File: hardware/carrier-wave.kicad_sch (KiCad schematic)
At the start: 4 parts, among them U2 OPA695, U3 THS3491, U4 AD9834, U7 TS5A3159ADCK

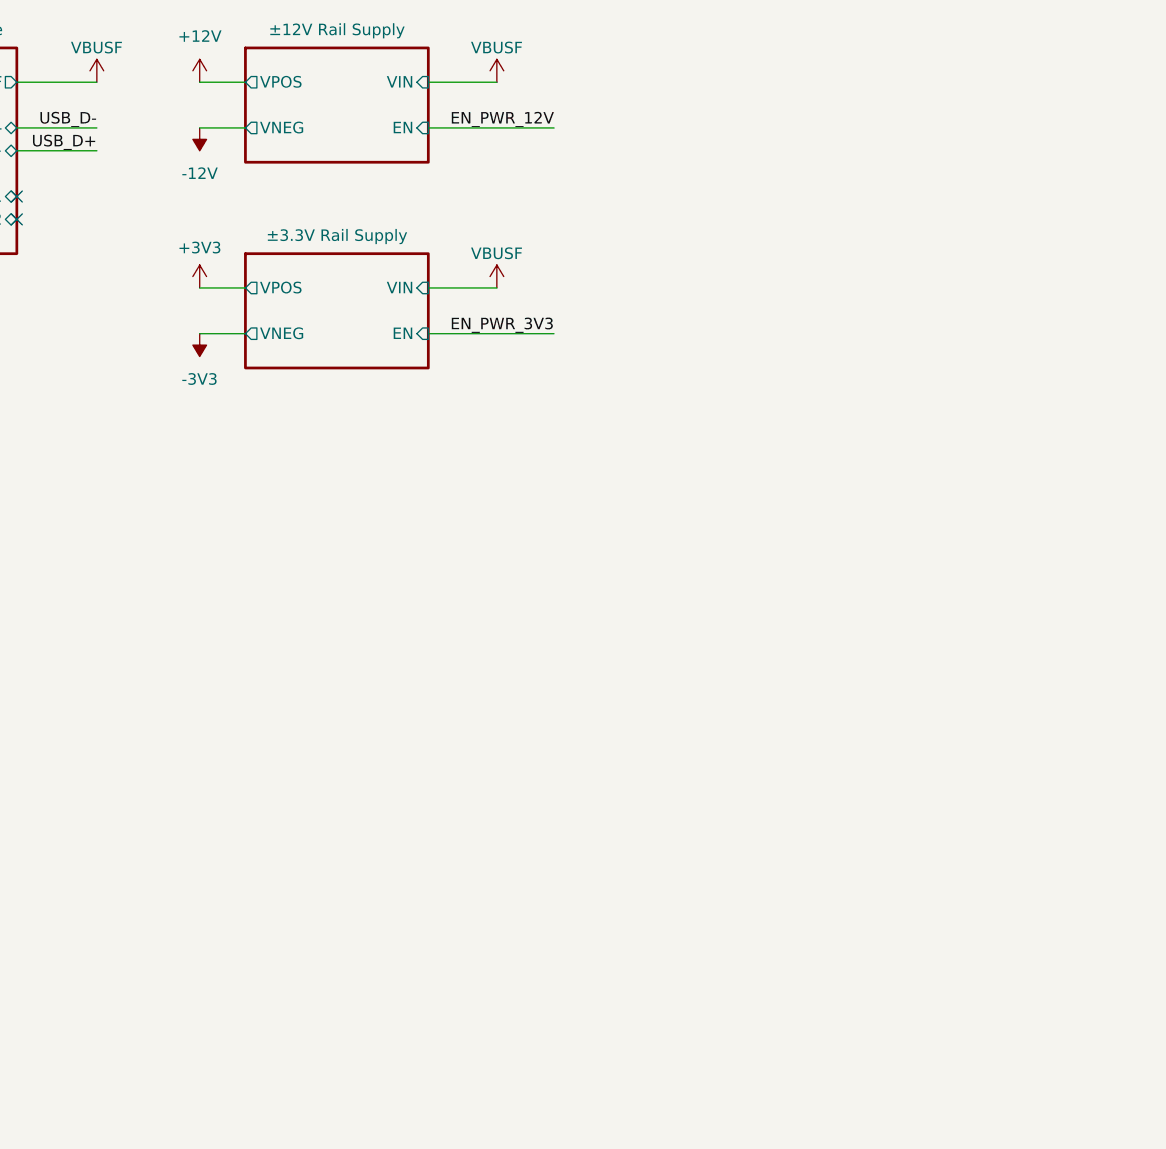
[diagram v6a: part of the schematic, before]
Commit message: Begin digital design
created sheets for MCU and 3.3VD regulator
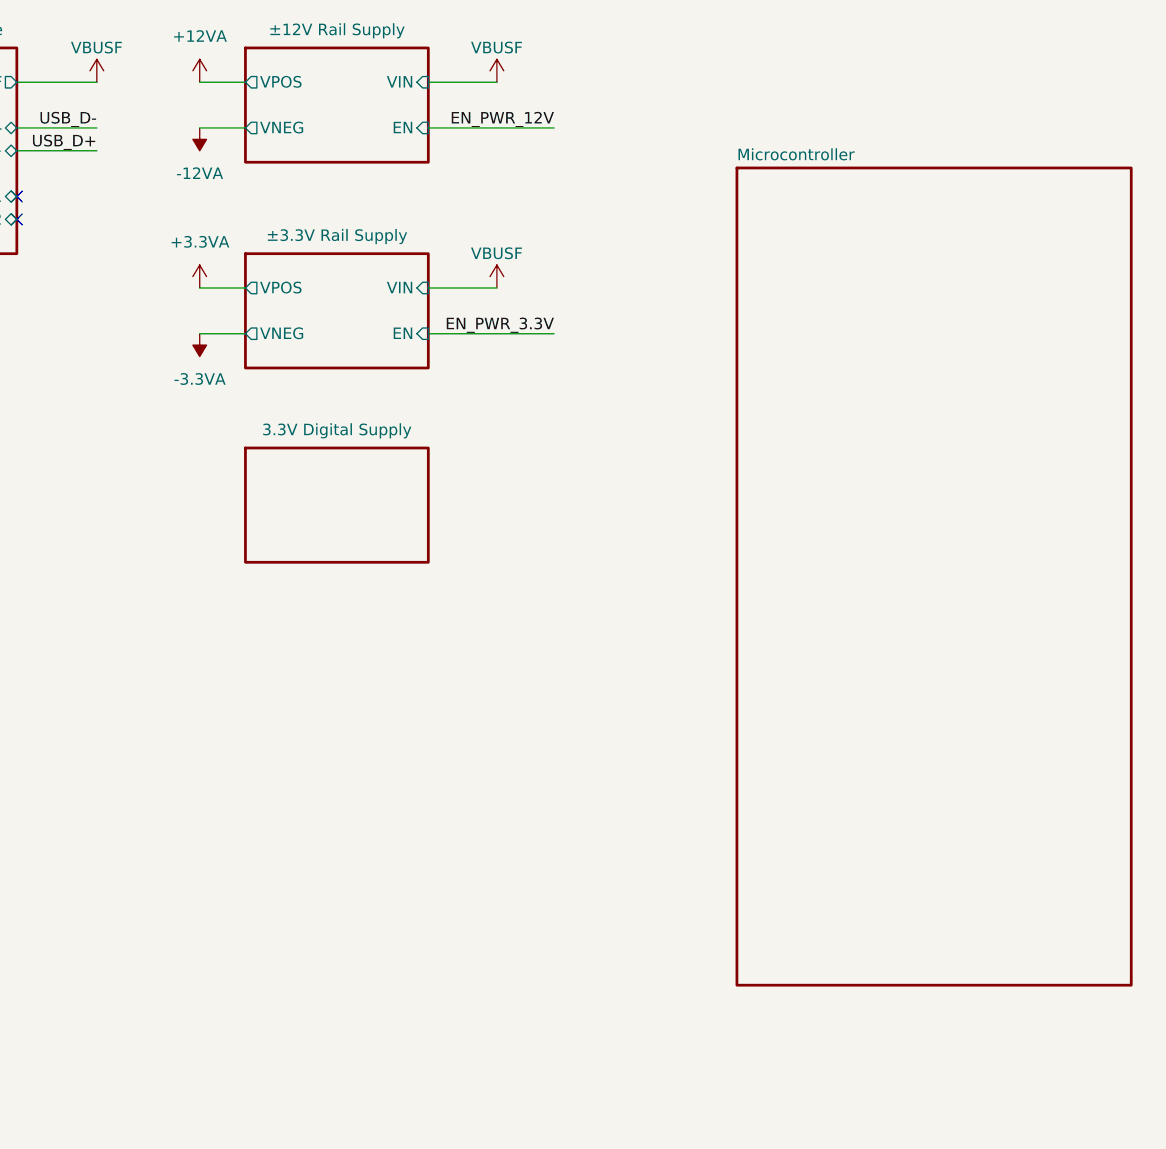
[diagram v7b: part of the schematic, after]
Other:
- added sheet 3.3V Digital Supply (3V_digital_supply.kicad_sch)
- added sheet Microcontroller (microcontroller.kicad_sch)
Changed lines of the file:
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@@
 		)
 	)
-	(label "EN_PWR_3V3"
+	(label "EN_PWR_3.3V"
 		(at 92.71 52.07 180)
 		(effects
@@
 			)
 		)
-		(property "Value" "-12V"
+		(property "Value" "-12VA"
 			(at 53.34 34.29 0)
 			(show_name no)
@@
 			)
 		)
-		(property "Value" "-3V3"
+		(property "Value" "-3.3VA"
 			(at 53.34 57.15 0)
 			(show_name no)
@@
 			)
 		)
-		(property "Value" "+3V3"
-			(at 53.34 42.545 0)
+		(property "Value" "+3.3VA"
+			(at 53.34 41.91 0)
 			(show_name no)
 			(do_not_autoplace no)
@@
 			)
 		)
-		(property "Value" "+12V"
+		(property "Value" "+12VA"
 			(at 53.34 19.05 0)
 			(show_name no)
@@
 	)
 	(sheet
-		(at 58.42 43.18)
+		(at 58.42 64.77)
 		(size 20.32 12.7)
 		(exclude_from_sim no)
@@
 			(color 255 229 191 1)
 		)
+		(property "Sheetname" "3.3V Digital Supply"
+			(at 68.58 63.5 0)
+			(show_name no)
+			(do_not_autoplace no)
+			(effects
+				(font
+					(size 1.27 1.27)
+				)
+				(justify bottom)
+			)
+		)
+		(property "Sheetfile" "3V_digital_supply.kicad_sch"
+			(at 58.42 78.1308 0)
+			(hide yes)
+			(show_name no)
+			(do_not_autoplace no)
+			(effects
+				(font
+					(size 1.27 1.27)
+				)
+				(justify left top)
+			)
+		)
+		(instances
+			(project "carrier-wave"
+				(path "/dc900721-a2e3-4f11-b4f2-59bb3a47422e"
+					(page "6")
+				)
+			)
+		)
+	)
+	(sheet
+		(at 58.42 43.18)
+		(size 20.32 12.7)
+		(exclude_from_sim no)
+		(in_bom yes)
+		(on_board yes)
+		(dnp no)
+		(stroke
+			(width 0.3048)
+			(type solid)
+		)
+		(fill
+			(color 255 229 191 1)
+		)
 		(property "Sheetname" "±3.3V Rail Supply"
 			(at 68.58 41.91 0)
@@
 				)
 			)
+		)
+	)
+	(sheet
+		(at 113.03 33.655)
+		(size 43.815 90.805)
+		(exclude_from_sim no)
+		(in_bom yes)
+		(on_board yes)
+		(dnp no)
+		(fields_autoplaced yes)
+		(stroke
+			(width 0.3048)
+			(type solid)
+		)
+		(fill
+			(color 255 229 191 1)
+		)
+		(property "Sheetname" "Microcontroller"
+			(at 113.03 32.9434 0)
+			(show_name no)
+			(do_not_autoplace no)
+			(effects
+				(font
+					(size 1.27 1.27)
+				)
+				(justify left bottom)
+			)
+		)
+		(property "Sheetfile" "microcontroller.kicad_sch"
+			(at 113.03 125.0446 0)
+			(hide yes)
+			(show_name no)
+			(do_not_autoplace no)
+			(effects
+				(font
+					(size 1.27 1.27)
+				)
+				(justify left top)
+			)
+		)
+		(instances
+			(project "carrier-wave"
+				(path "/dc900721-a2e3-4f11-b4f2-59bb3a47422e"
+					(page "5")
+				)
+			)

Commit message: Finalize power
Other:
- removed sheet Microcontroller
- sheet USB C Interface ports: added ~{EN}, ~{FAULT}; removed VBUSF
- sheet ±12V Rail Supply ports: added none; removed VIN, VNEG, VPOS
- sheet ±3.3V Rail Supply ports: added PG; removed VIN, VNEG, VPOS
